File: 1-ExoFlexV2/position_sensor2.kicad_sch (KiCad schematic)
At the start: 25 parts, among them U54 SN74LVC3G14DCUT_V2, U55 SN74LVC3G14DCUT_V2, U56 SN74LVC3G14DCUT_V2, U57 SN74LVC1G08DBVR, U58 SN74LVC1G08DBVR, U59 SN74LVC3G14DCUT_V2

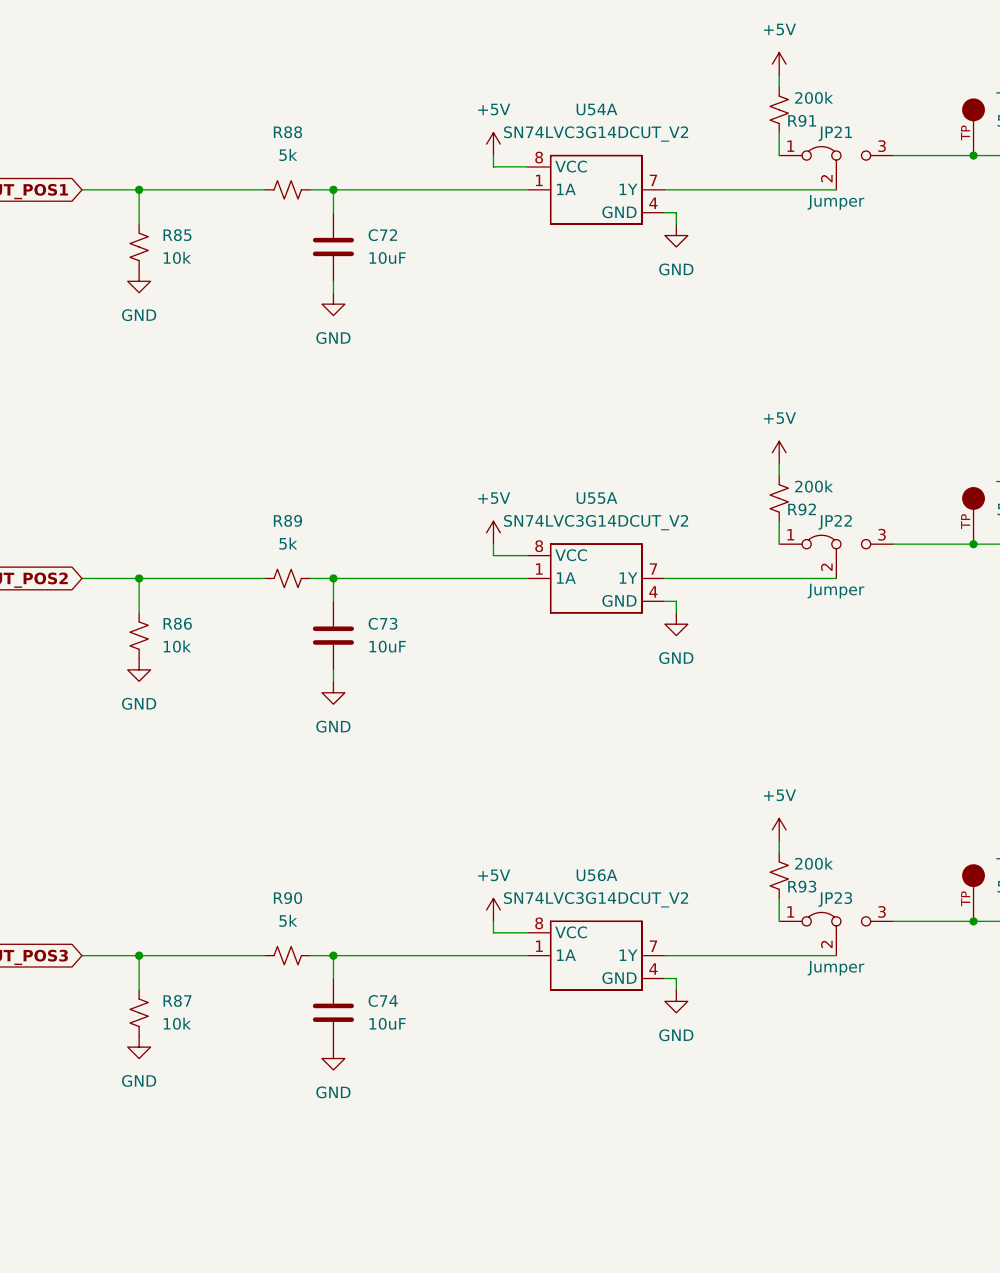
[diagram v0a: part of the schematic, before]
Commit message: Chokes et RC
- Ajout des RF chokes
- Changement des résistance pour 0805
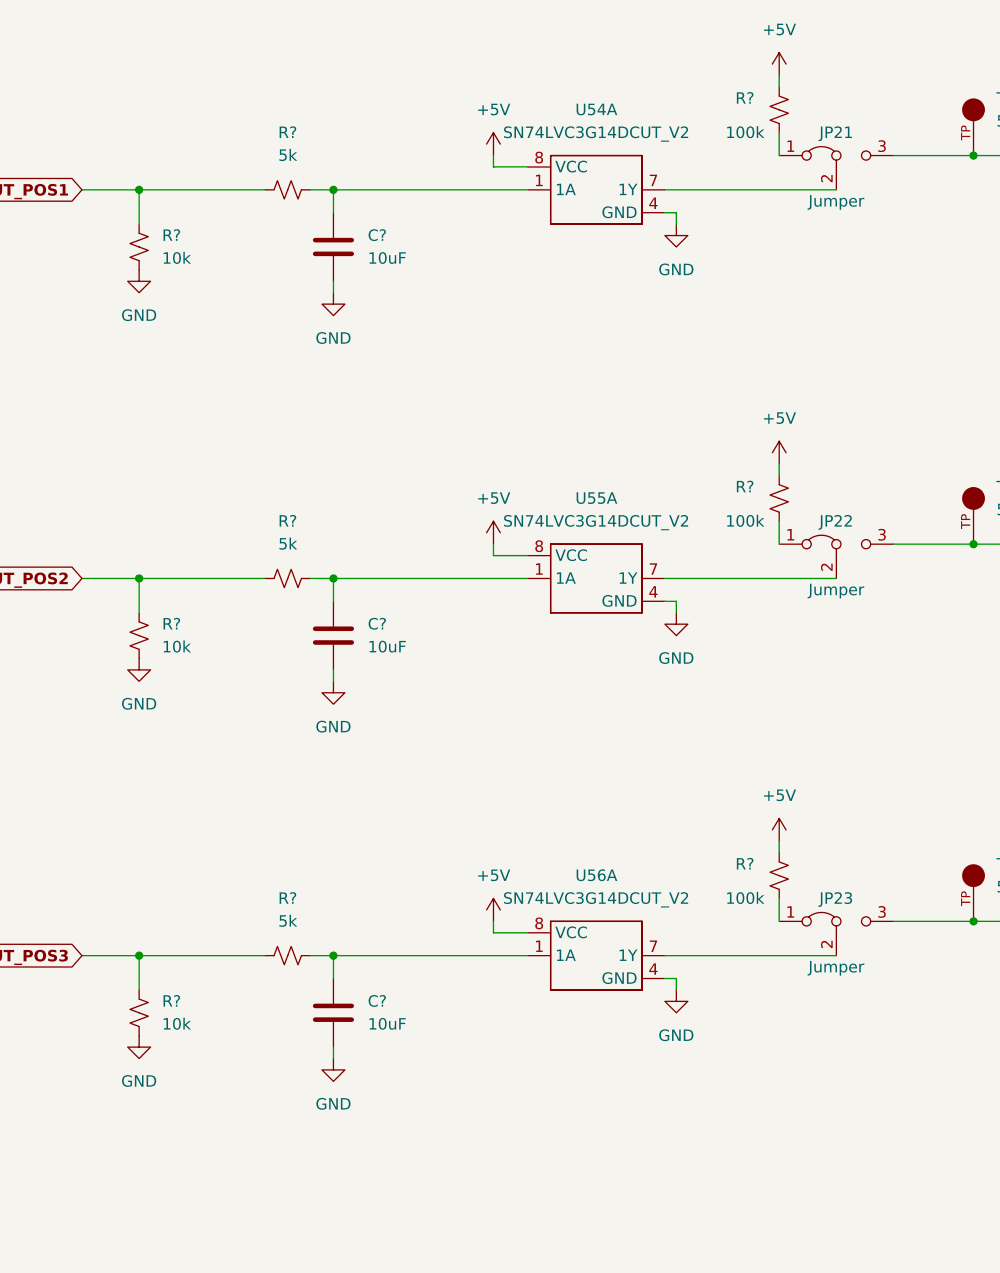
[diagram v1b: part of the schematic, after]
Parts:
- removed C72, C73, C74: 10uF, Capacitor_SMD:C_0603_1608Metric, symbol Device:C
- removed R85, R86, R87: 10k, Resistor_SMD:R_0603_1608Metric, symbol Device:R_Small_US
- removed R88, R89, R90: 5k, Resistor_SMD:R_0603_1608Metric, symbol Device:R_Small_US
- removed R91, R92, R93: 200k, Resistor_SMD:R_0603_1608Metric, symbol Device:R_Small_US
- added C? (x3): 10uF, Capacitor_SMD:C_0805_2012Metric, symbol Device:C
- added R? (x3): 100k, Resistor_SMD:R_0805_2012Metric, symbol Device:R_Small_US
- added R? (x3): 5k, Resistor_SMD:R_0805_2012Metric, symbol Device:R_Small_US
- added R? (x3): 10k, Resistor_SMD:R_0805_2012Metric, symbol Device:R_Small_US
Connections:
- net +5V: now also R?.1, R?.1, R?.1
- net BUT_POS1: now also R?.1, R?.1
- net BUT_POS2: now also R?.1, R?.1
- net BUT_POS3: now also R?.1, R?.1
- net GND: now also C?.2, C?.2, C?.2, R?.2, R?.2, R?.2
- net at JP23.1 (A): now also R?.2
- net at U56.1 (1A): now also C?.1, R?.2
- net at U55.1 (1A): now also C?.1, R?.2
- net at JP22.1 (A): now also R?.2
- net at U54.1 (1A): now also C?.1, R?.2
- net at JP21.1 (A): now also R?.2

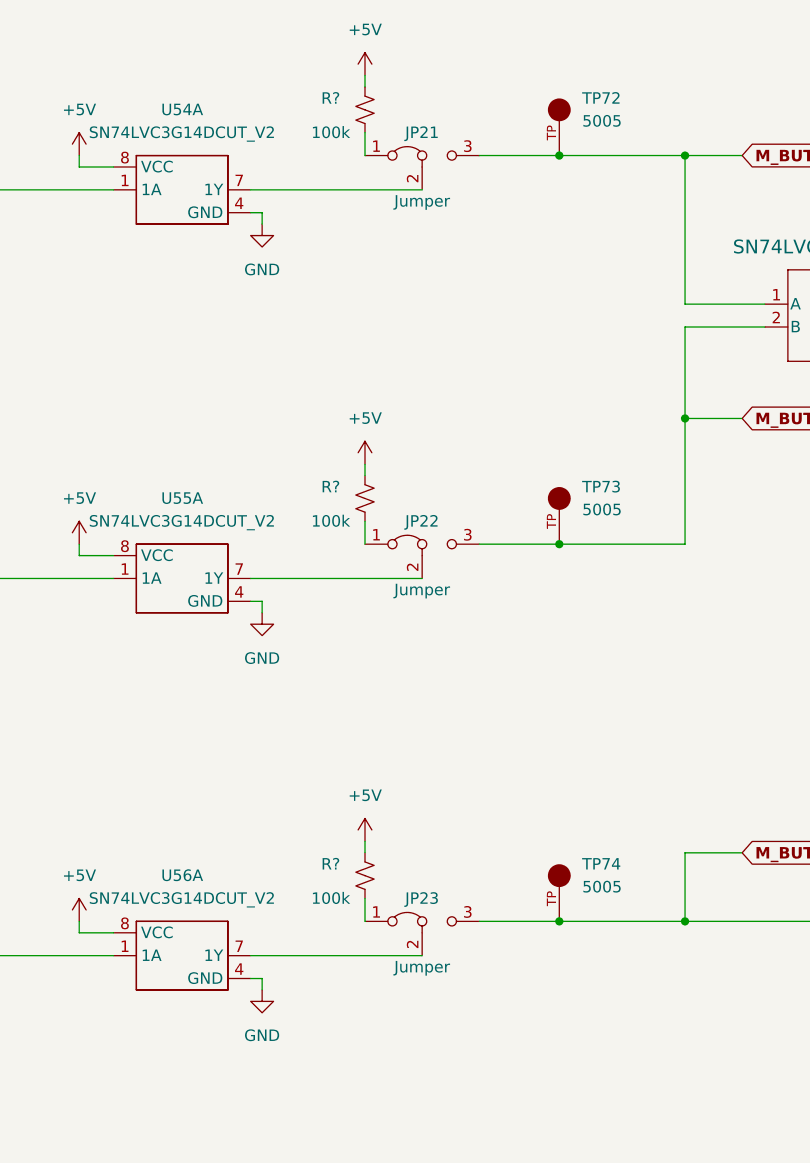
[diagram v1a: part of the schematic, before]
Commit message: Trimmer et jumper
-Changement de symbole de jumper
-Ajout des des trimmer aux endroits nécessaires
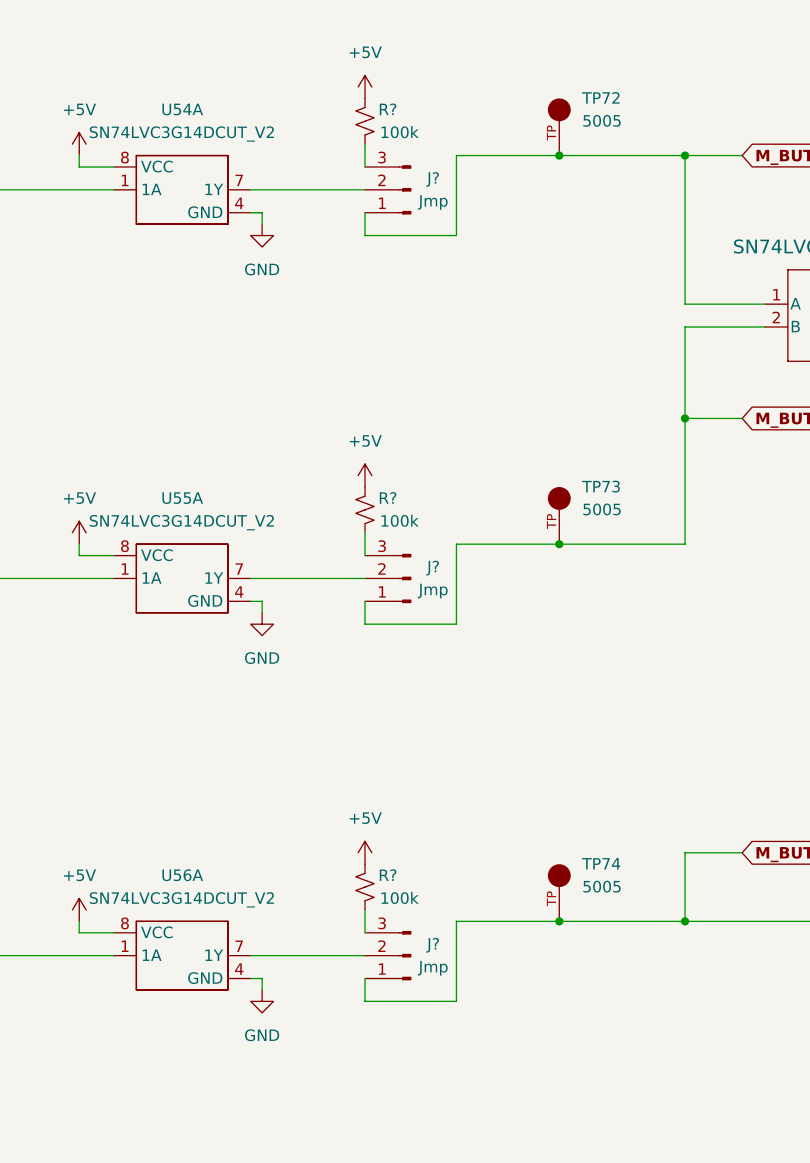
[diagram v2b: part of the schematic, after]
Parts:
- removed JP21, JP22, JP23: Jumper, Connector_PinHeader_2.54mm:PinHeader_1x03_P2.54mm_Vertical, symbol Jumper:Jumper_3_Bridged12
- removed R? (x3): 100k, Resistor_SMD:R_0805_2012Metric, symbol Device:R_Small_US
- added J? (x3): Jmp, symbol Connector:Conn_01x03_Male
- added R? (x3): 100k, Resistor_SMD:R_0805_2012Metric, symbol Device:R_Small_US
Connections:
- net +5V: now also R?.2, R?.2, R?.2
- net M_BUT_POS1: now also J?.1 (Pin_1)
- net M_BUT_POS2: now also J?.1 (Pin_1)
- net M_BUT_POS3: now also J?.1 (Pin_1)
- net at U56.7 (1Y): now also J?.2 (Pin_2)
- net at U55.7 (1Y): now also J?.2 (Pin_2)
- net at U54.7 (1Y): now also J?.2 (Pin_2)
- new net: J?.3 (Pin_3), R?.1 (x3)

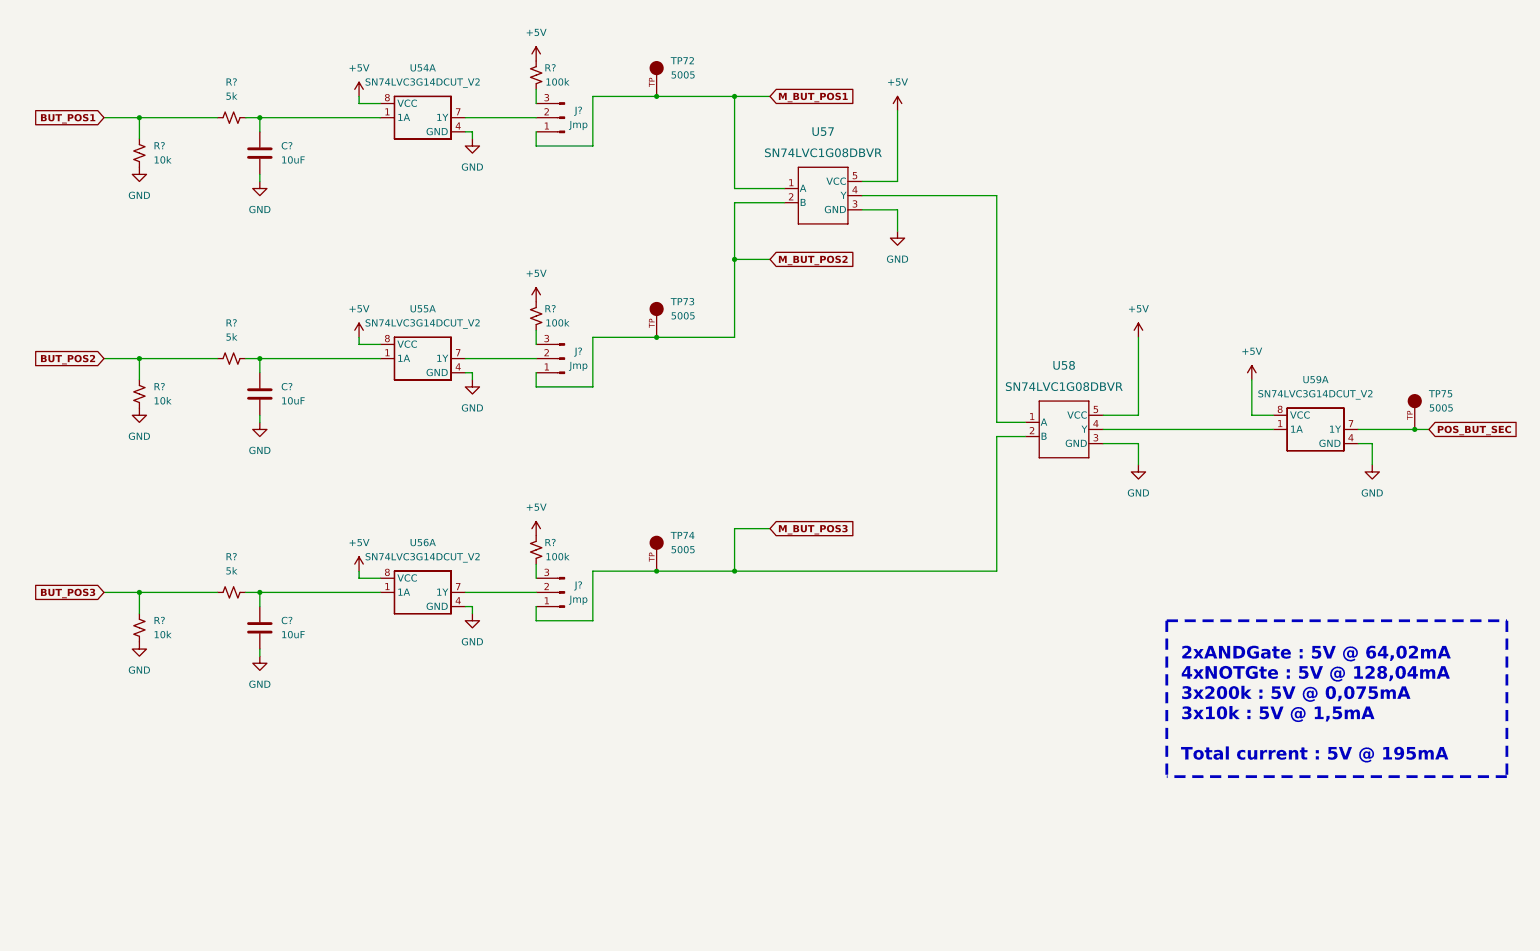
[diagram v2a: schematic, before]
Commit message: Test points et notes
- Ajout de tous les tests point nécessaires
-  Ajoute des sections de notes dans chaque page
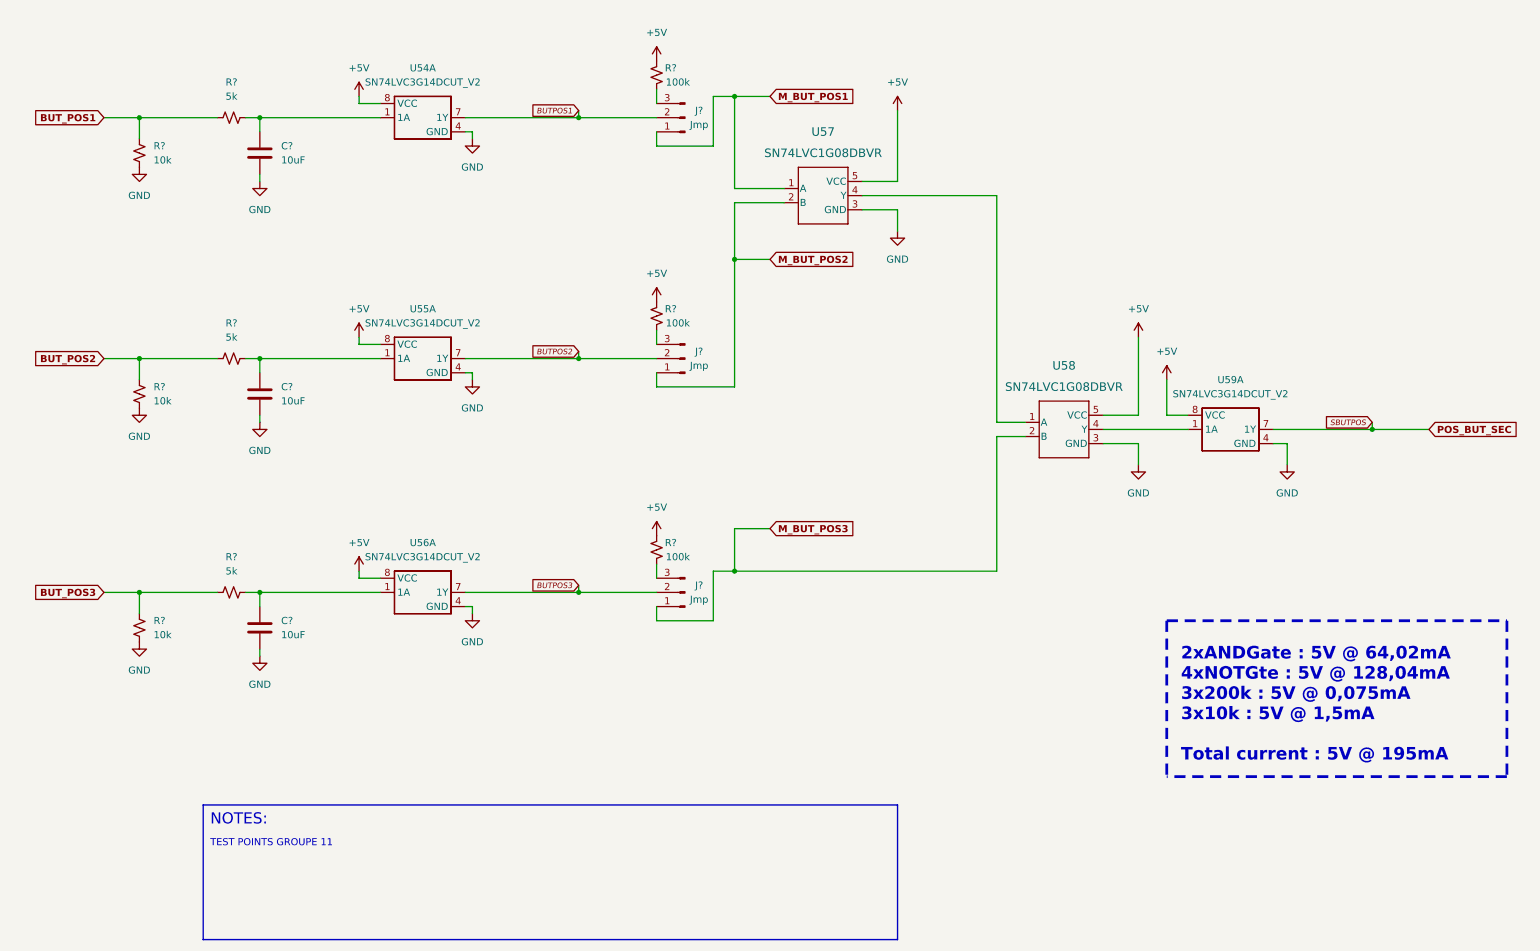
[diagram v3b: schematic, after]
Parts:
- removed TP72, TP73, TP74, TP75: 5005, FootPrint:KEYSTONE_5005, symbol SymLib:5005
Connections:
- net BUTPOS2: now reaches J?.2 (Pin_2), U55.7 (1Y)
- net BUTPOS1: now reaches J?.2 (Pin_2), U54.7 (1Y)
- net BUTPOS3: now reaches J?.2 (Pin_2), U56.7 (1Y)
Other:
- note added: "NOTES:"
- note added: "TEST POINTS GROUPE 11"
- moved on the sheet: J?, R?, U59A

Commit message: Schématisation terminée
- Schéma terminé
- Passage vers le PCB
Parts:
- C46, C47, C48: renamed from C?; value 10uF -> 10uF 10V X7R; DESCRIPTION (none) -> 10 µF ±10% 10V Ceramic Capacitor X7R 0805 (2012 Metric); MANUFACTURER (none) -> Murata Electronics; PACKAGE (none) -> 0805 (2012 Metric); PART NUMBER (none) -> GRM21BR71A106KA73L; TYPE (none) -> SMD
- J103, J104, J105: renamed from J?; value Jmp -> Jumper; footprint (none) -> Connector_PinSocket_2.54mm:PinSocket_1x03_P2.54mm_Vertical; DESCRIPTION (none) -> CONN HEADER VERT 3POS 2.54MM; MANUFACTURER (none) -> Würth Elektronik; PACKAGE (none) -> Square 0.100" (2.54mm); PART NUMBER (none) -> 61300311121; TYPE (none) -> Through Hole
- R146, R147, R148: renamed from R?; value 10k -> 10k 5% 1/8W; DESCRIPTION (none) -> 10 kOhms ±5% 0.125W, 1/8W Chip Resistor 0805 (2012 Metric) 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; MANUFACTURER (none) -> Panasonic Electronic Components; PACKAGE (none) -> 0805 (2012 Metric); PART NUMBER (none) -> ERJ-6GEYJ103V; TYPE (none) -> SMD
- R149, R150, R151: renamed from R?; value 5k -> 5,1k 5% 1/8W; DESCRIPTION (none) -> 5.1 kOhms ±5% 0.125W, 1/8W Chip Resistor 0805 (2012 Metric)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; MANUFACTURER (none) -> Panasonic Electronic Components; PACKAGE (none) -> 0805 (2012 Metric); PART NUMBER (none) -> ERJ-6GEYJ512V; TYPE (none) -> SMD
- R152, R153, R154: renamed from R?; value 100k -> 100k 5% 1/8W; DESCRIPTION (none) -> 100 kOhms ±5% 0.125W, 1/8W Chip Resistor 0805 (2012 Metric)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; MANUFACTURER (none) -> Panasonic Electronic Components; PACKAGE (none) -> 0805 (2012 Metric); PART NUMBER (none) -> ERJ-6GEYJ104V; TYPE (none) -> SMD
- U73: renamed from U54; value SN74LVC3G14DCUT_V2 -> Inverter; DESCRIPTION (none) -> Inverter IC 3 Channel Schmitt Trigger 8-VSSOP; MANUFACTURER (none) -> Texas Instruments; PACKAGE (none) -> 8-VFSOP (0.091", 2.30mm Width); PART NUMBER (none) -> SN74LVC3G14DCUT; TYPE (none) -> SMD
- U74: renamed from U55; value SN74LVC3G14DCUT_V2 -> Inverter; DESCRIPTION (none) -> Inverter IC 3 Channel Schmitt Trigger 8-VSSOP; MANUFACTURER (none) -> Texas Instruments; PACKAGE (none) -> 8-VFSOP (0.091", 2.30mm Width); PART NUMBER (none) -> SN74LVC3G14DCUT; TYPE (none) -> SMD
- U75: renamed from U56; value SN74LVC3G14DCUT_V2 -> Inverter; DESCRIPTION (none) -> Inverter IC 3 Channel Schmitt Trigger 8-VSSOP; MANUFACTURER (none) -> Texas Instruments; PACKAGE (none) -> 8-VFSOP (0.091", 2.30mm Width); PART NUMBER (none) -> SN74LVC3G14DCUT; TYPE (none) -> SMD
- U76: renamed from U57; value SN74LVC1G08DBVR -> AND Gate; DESCRIPTION (none) -> AND Gate IC 1 Channel SOT-23-5; MANUFACTURER (none) -> Texas Instruments; PACKAGE (none) -> SC-74A, SOT-753; PART NUMBER (none) -> SN74LVC1G08DBVR; TYPE (none) -> SMD
- U77: renamed from U58; value SN74LVC1G08DBVR -> AND Gate; DESCRIPTION (none) -> AND Gate IC 1 Channel SOT-23-5; MANUFACTURER (none) -> Texas Instruments; PACKAGE (none) -> SC-74A, SOT-753; PART NUMBER (none) -> SN74LVC1G08DBVR; TYPE (none) -> SMD
- U78: renamed from U59; value SN74LVC3G14DCUT_V2 -> Inverter; DESCRIPTION (none) -> Inverter IC 3 Channel Schmitt Trigger 8-VSSOP; MANUFACTURER (none) -> Texas Instruments; PACKAGE (none) -> 8-VFSOP (0.091", 2.30mm Width); PART NUMBER (none) -> SN74LVC3G14DCUT; TYPE (none) -> SMD
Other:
- note added: "2xANDGate : 5V @ 64,02mA 4xNOTGte : 5V @ 128,04mA 3x100k : 5V @ 0,15mA 3x10k : 5V @ 1,5mA Total current : 5V @ 198mA"
- note removed: "2xANDGate : 5V @ 64,02mA 4xNOTGte : 5V @ 128,04mA 3x200k : 5V @ 0,075mA 3x10k : 5V @ 1,5mA Total current : 5V @ 195mA"
- moved on the sheet: J103, J104, J105, R152, R153, R154
